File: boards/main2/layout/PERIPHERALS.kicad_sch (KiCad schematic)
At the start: 30 parts, among them Q1 AO3400A, SW1 DSHP04TJGER, SW2 GT-TC048B-H025-L1, SW3 GT-TC048B-H025-L1, SW5 GT-TC048B-H025-L1, U2 GT-USB-7010ASV, U6 USBLC6-2SC6

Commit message: 🍱 Regenerate main2's DRIVERS and PERIPHERALS sheets with the widened USBLC6 and the jumper pin labels
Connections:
- net USBD_N: now also U6.4 (I/O2)
- net USBD_P: now also U6.6 (I/O1)
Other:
- note added: "Addressable LEDs: WS2812C-2020 chain"
- note added: "Buttons: user, reset (NRST), boot (BOOT0)"
- note added: "Buzzer: FUET-5030, low-side switch Q1"
- note added: "Sheet ports"
- note added: "Status LEDs"
- note added: "Strategy DIP switch"
- note added: "USB-C receptacle (ESP32 USB), VBUS sense, ESD"
- title: (none) -> User interface and USB-C
- moved on the sheet: BZ1, C18, C19, C20, C21, C60, C79, D1, D2, D3, D4, D5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

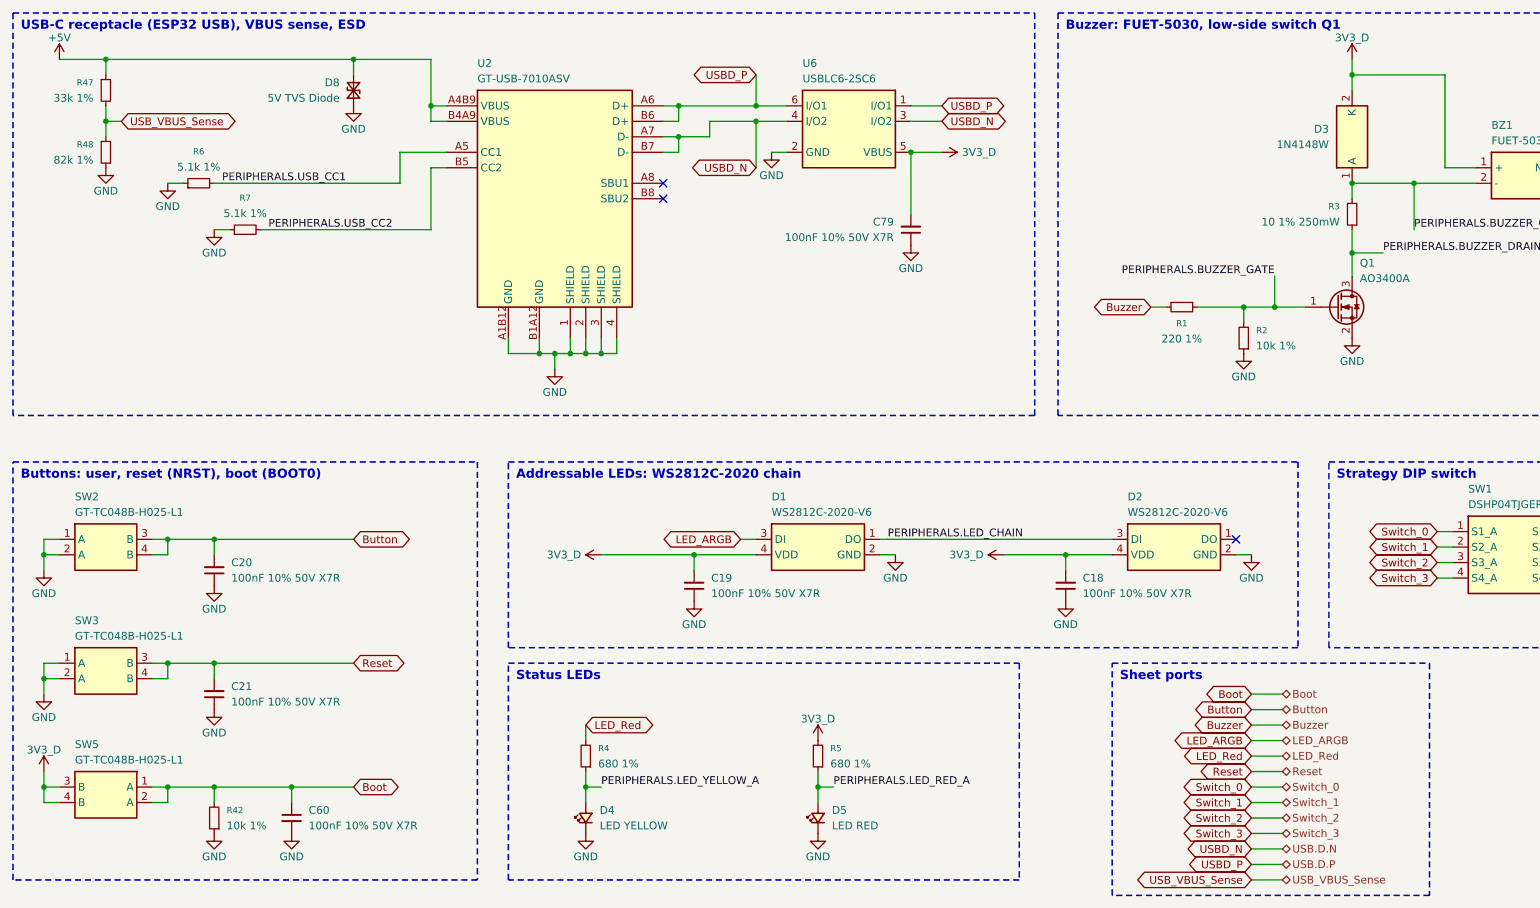
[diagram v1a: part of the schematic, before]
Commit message: ✨ Set main2's emitter current from the DAC and AC-couple its selectors
- The shared sink's set-point comes from PA5 (DAC1_OUT2, buffer off) through
  200k/20k, ratiometric to VDDA and 0 V at reset; 1k/1 nF compensates the loop
  into Q9 and 200k from 3V3_A turns the sink off at a zero set-point.
- Q2-Q5 keep the main board's AC-coupled gates (220 nF, 22k, 1N4148WS clamp):
  a pin held high turns its emitter off within 11 ms.
- Battery_Voltage moves to PC5, Switch_0 to PH0; the H7's VBUS divider goes,
  the ESP32 reports USB power over UART4.
- A test bench checks the selector coupling and the DAC set-point; the
  research model is calculations/emitter/emitter_sink.py.
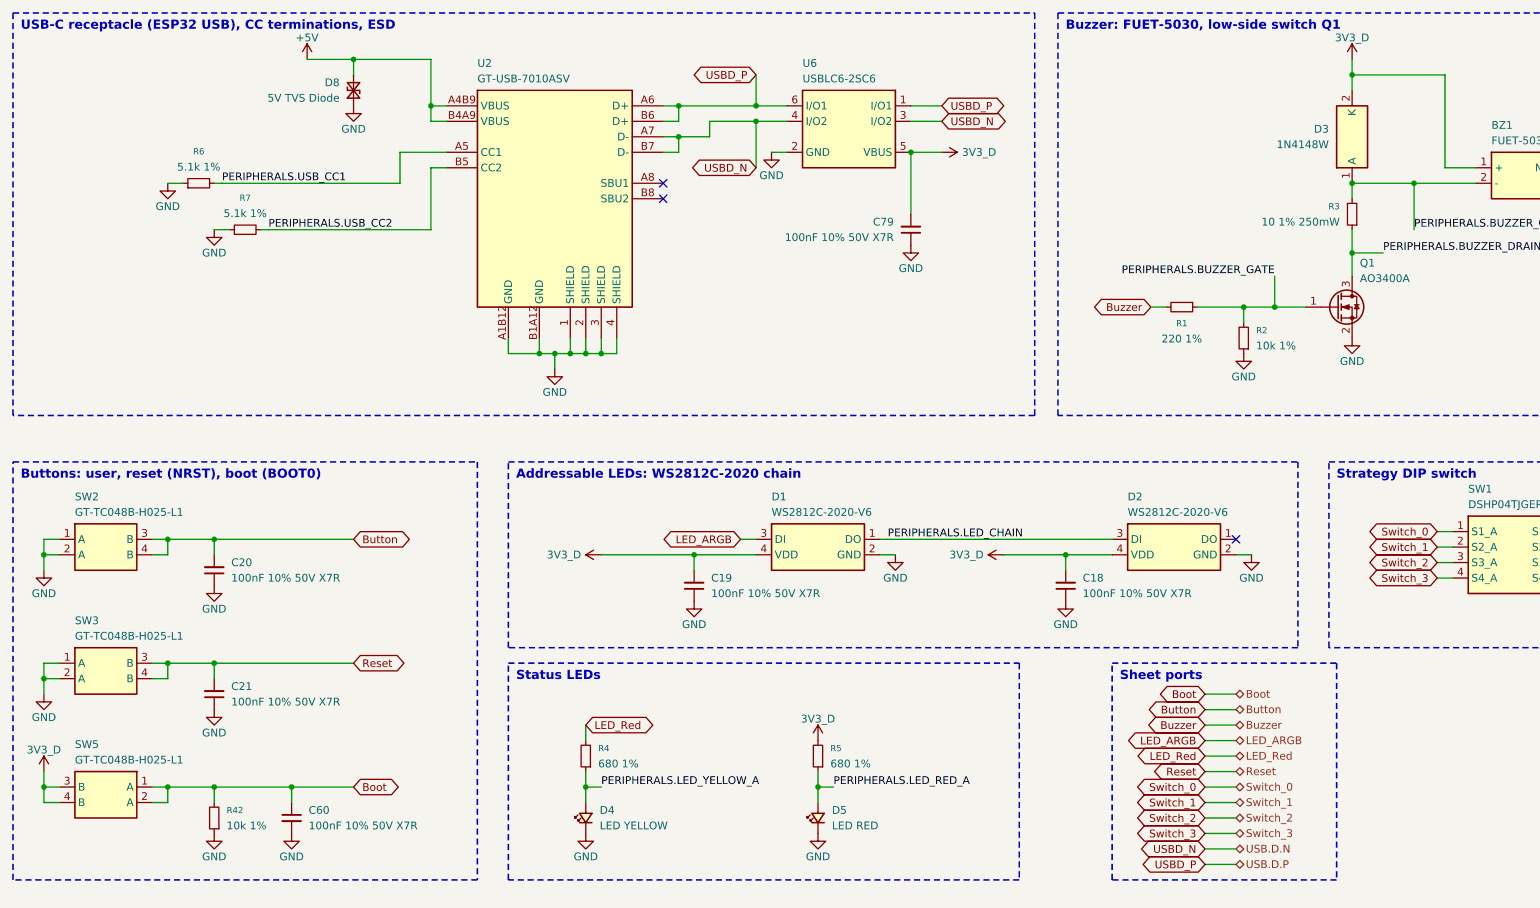
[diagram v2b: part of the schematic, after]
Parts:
- removed R47: 33k 1%, stdlib_kicad-footprints_Resistor_SMD:R_0402_1005Metric, symbol R_Small
- removed R48: 82k 1%, stdlib_kicad-footprints_Resistor_SMD:R_0402_1005Metric, symbol R_Small
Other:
- note added: "USB-C receptacle (ESP32 USB), CC terminations, ESD"
- note removed: "USB-C receptacle (ESP32 USB), VBUS sense, ESD"

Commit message: 🚧 Place and route main2 but for 12 connections
place.py places every part and route.py pours the planes and routes the board, with hand-routed
fixes on top. 12 connections are still open (boards/main2/layout/README.md, Layout), so DRC and
the layout check fail on them; every other gate passes.
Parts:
- removed SW5: GT-TC048B-H025-L1, Team-Micras_MicrasPCB_components_g-switch_GT-TC048B-H025-L1:SW-SMD-4P_L4.2-W3.2_GT-TC048, symbol GT-TC048B-H025-L1
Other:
- note added: "Buttons: user, reset (NRST); BOOT0 pull-down"
- note removed: "Buttons: user, reset (NRST), boot (BOOT0)"

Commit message: 🐛 Fix main2's review findings and settle its open doubts
Schematic and parts:
- Battery input: F1 is a 12 A Littelfuse 501 (0501012.WR1). C58 now sits
  gate-source with C114 gate-drain, so Q6 stays off at plug-in. D16 clamps
  Q8's VGS. R44/R45 are 10k/2k, so VBAT can't float up on USB alone.
- Capacitors: VBAT and VSYS use 1210/0805 50 V parts, sized with Samsung's
  DC-bias curves. C109 is fitted.
- Drivers: R66/R76 are removed (the chokes are needed). ITRIP and the fan
  limit are retuned. The INA241 R_iso is 150 Ohm.
- Rails are declared as ranges, and the abs-max checks run under the TVS
  clamp.
- STM32 pin swaps for routing: the wall selectors move to TIM3,
  Motor_Left_EN to TIM8_CH2 and LED_ARGB to TIM17. CubeMX 6.18.1 confirms
  the map.
- firmware_changes.toml registers the matching firmware changes: the ADC
  0.7 us sampling time, the TIM4-triggered DAC, the fan's 50 kHz start, a
  wheel-sign self-check, VDDA tracking, contest mode, the debug halt and
  others.

Layout:
- USB D+/D- are routed as a coupled pair. The track floor is 0.12 mm.
- Stubs and detours are trimmed. The In2 VCORE/3V3_D islands are shrunk.
- The board is notched under the ESP32 antenna.
- Ground stitching, thermal reliefs, open thermal vias with split paste,
  DRV8874 heat islands and teardrops are added.
- 11 joins remain for hand-routing (layout README, Open items).

Doubts are closed by datasheets, vendor SPICE models and new research
calculations instead of bench TODOs. Tests cover each review item.
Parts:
- D3: value 1N4148W -> 1N4148WS; footprint Team-Micras_MicrasPCB_components_hongjiacheng_1N4148W:SOD-123_L2.7-W1.6-LS3.7-FD -> Team-Micras_MicrasPCB_components_cj_1N4148WS:D_SOD-323; symbol 1N4148W -> 1N4148WS
- D8: value 5V TVS Diode -> 6V TVS Diode
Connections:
- net 3V3_D: now also D3.1 (K); no longer D3.2 (K)
- net PERIPHERALS.BUZZER_COIL: now also D3.2 (A); no longer D3.1 (A)
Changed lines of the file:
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@@
 	)
 	(symbol
-		(lib_id "1N4148W")
+		(lib_id "1N4148WS")
 		(at 229.87 33.02 90)
 		(unit 1)
@@
 			)
 		)
-		(property "Value" "1N4148W"
+		(property "Value" "1N4148WS"
 			(at 226.06 34.29 90)
 			(show_name no)
@@
 			)
 		)
-		(property "Footprint" "Team-Micras_MicrasPCB_components_hongjiacheng_1N4148W:SOD-123_L2.7-W1.6-LS3.7-FD"
+		(property "Footprint" "Team-Micras_MicrasPCB_components_cj_1N4148WS:D_SOD-323"
 			(at 229.87 33.02 90)
 			(hide yes)
@@
 			)
 		)
-		(property "Datasheet" "https://www.lcsc.com/product-detail/C7420318.html"
+		(property "Datasheet" "https://www.lcsc.com/datasheet/lcsc_datasheet_1810101110_Jiangsu-Changjing-Electronics-Technology-Co---Ltd--1N4148WS_C2128.pdf"
 			(at 229.87 33.02 90)
 			(hide yes)
@@
 			)
 		)
-		(property "Description" "Fast switching diode, 100 V, 150 mA, trr 4 ns, SOD-123 (pad 1 anode, pad 2 cathode)"
+		(property "Description" "Fast switching diode, 100 V, 150 mA, trr 4 ns, SOD-323 (pad 1 cathode, pad 2 anode)"
 			(at 229.87 33.02 90)
 			(hide yes)
@@
 			)
 		)
-		(property "Value" "5V TVS Diode"
+		(property "Value" "6V TVS Diode"
 			(at 63.754 26.67 90)
 			(show_name no)
@@
 			)
 		)
-		(property "Description" "5V TVS Diode"
+		(property "Description" "6V TVS Diode"
 			(at 66.04 25.4 90)
 			(hide yes)

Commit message: 🎨 Draw the diodes and buzzer as symbols, and make D4 blue
- 1N4148WS, B5819W and FUET-5030: replace the box bodies with diode,
  Schottky and buzzer symbols (same pins). Nudge D3 and BZ1 on both boards'
  PERIPHERALS sheets.
- D4: KENTO KT-0603B blue (C2288, VF 2.6-3.1 V at 5 mA) instead of the
  yellow NCD0603Y2. R4 goes from 680 Ohm to 100 Ohm: 1.2 mA at the worst
  bin and rail, 7.5 mA at most. LED_YELLOW_A is renamed LED_BLUE_A.
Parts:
- D4: value LED YELLOW -> LED BLUE; symbol LED_Small_Filled_Yellow -> LED_Small_Filled_Blue
- R4: value 680 1% -> 100 1%
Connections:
- net PERIPHERALS.LED_YELLOW_A renamed PERIPHERALS.LED_BLUE_A
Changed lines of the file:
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@@
 	(symbol
 		(lib_id "FUET-5030")
-		(at 257.81 40.64 0)
+		(at 257.81 38.1 0)
 		(unit 1)
 		(body_style 1)
@@
 		(dnp no)
 		(property "Reference" "BZ1"
-			(at 252.73 31.115 0)
+			(at 256.159 30.48 0)
 			(show_name no)
 			(do_not_autoplace no)
@@
 		)
 		(property "Value" "FUET-5030"
-			(at 252.73 33.655 0)
+			(at 256.159 33.02 0)
 			(show_name no)
 			(do_not_autoplace no)
@@
 		)
 		(property "Footprint" "Team-Micras_MicrasPCB_components_fuet_FUET-5030:BUZ-SMD_FST-5030"
-			(at 257.81 40.64 0)
+			(at 257.81 38.1 0)
 			(hide yes)
 			(show_name no)
@@
 		)
 		(property "Datasheet" "https://www.lcsc.com/product-detail/C391031.html"
-			(at 257.81 40.64 0)
+			(at 257.81 38.1 0)
 			(hide yes)
 			(show_name no)
@@
 		)
 		(property "Description" "4 kHz passive electromagnetic buzzer, 3 Vo-p rated, 12 ohm coil, 5 x 5 x 3 mm SMD (pad 3 mechanical, no electrical function stated)"
-			(at 257.81 40.64 0)
+			(at 257.81 38.1 0)
 			(hide yes)
 			(show_name no)
@@
 		)
 		(property "Path" "PERIPHERALS.BZ1.BUZZER"
-			(at 257.81 40.64 0)
+			(at 257.81 38.1 0)
 			(hide yes)
 			(show_name no)
@@
 	)
 	(symbol
-		(lib_id "LED_Small_Filled_Yellow")
+		(lib_id "LED_Small_Filled_Blue")
 		(at 104.14 144.78 90)
 		(unit 1)
@@
 			)
 		)
-		(property "Value" "LED YELLOW"
+		(property "Value" "LED BLUE"
 			(at 106.426 146.05 90)
 			(show_name no)
@@
 			)
 		)
-		(property "Description" "LED YELLOW"
+		(property "Description" "LED BLUE"
 			(at 104.14 144.78 90)
 			(hide yes)
@@
 			)
 		)
-		(property "Value" "680 1%"
+		(property "Value" "100 1%"
 			(at 106.172 135.89 0)
 			(show_name no)
@@
 			)
 		)
-		(property "Description" "680 1%"
+		(property "Description" "100 1%"
 			(at 104.14 134.62 0)
 			(hide yes)
@@
 	(symbol
 		(lib_id "1N4148WS")
-		(at 229.87 33.02 90)
+		(at 229.87 36.83 90)
 		(unit 1)
 		(body_style 1)
@@
 		(dnp no)
 		(property "Reference" "D3"
-			(at 226.06 31.75 90)
+			(at 227.33 35.56 90)
 			(show_name no)
 			(do_not_autoplace no)
@@
 		)
 		(property "Value" "1N4148WS"
-			(at 226.06 34.29 90)
+			(at 227.33 38.1 90)
 			(show_name no)
 			(do_not_autoplace no)
@@
 		)
 		(property "Footprint" "Team-Micras_MicrasPCB_components_cj_1N4148WS:D_SOD-323"
-			(at 229.87 33.02 90)
+			(at 229.87 36.83 90)
 			(hide yes)
 			(show_name no)
@@
 		)
 		(property "Datasheet" "https://www.lcsc.com/datasheet/lcsc_datasheet_1810101110_Jiangsu-Changjing-Electronics-Technology-Co---Ltd--1N4148WS_C2128.pdf"
-			(at 229.87 33.02 90)
+			(at 229.87 36.83 90)
 			(hide yes)
 			(show_name no)
@@
 		)
 		(property "Description" "Fast switching diode, 100 V, 150 mA, trr 4 ns, SOD-323 (pad 1 cathode, pad 2 anode)"
-			(at 229.87 33.02 90)
+			(at 229.87 36.83 90)
 			(hide yes)
 			(show_name no)
@@
 		)
 		(property "Path" "PERIPHERALS.D3.D"
-			(at 229.87 33.02 90)
+			(at 229.87 36.83 90)
 			(hide yes)
 			(show_name no)
@@
 	)
 	(no_connect
-		(at 265.43 38.1)
+		(at 262.89 38.1)
 	)
 	(no_connect
@@
 	(wire
 		(pts
-			(xy 229.87 25.4) (xy 229.87 22.86)
+			(xy 229.87 33.02) (xy 229.87 22.86)
 		)
 		(stroke
@@
 	(wire
 		(pts
-			(xy 250.19 38.1) (xy 245.11 38.1)
+			(xy 255.27 35.56) (xy 245.11 35.56)
 		)
 		(stroke
@@
 	(wire
 		(pts
-			(xy 245.11 38.1) (xy 245.11 22.86)
+			(xy 245.11 35.56) (xy 245.11 22.86)
 		)
 		(stroke
@@
 	(wire
 		(pts
-			(xy 250.19 40.64) (xy 240.03 40.64)
+			(xy 255.27 40.64) (xy 240.03 40.64)
 		)
 		(stroke
@@
 		)
 	)
-	(label "PERIPHERALS.LED_YELLOW_A"
+	(label "PERIPHERALS.LED_BLUE_A"
 		(at 106.68 139.7 0)
 		(effects

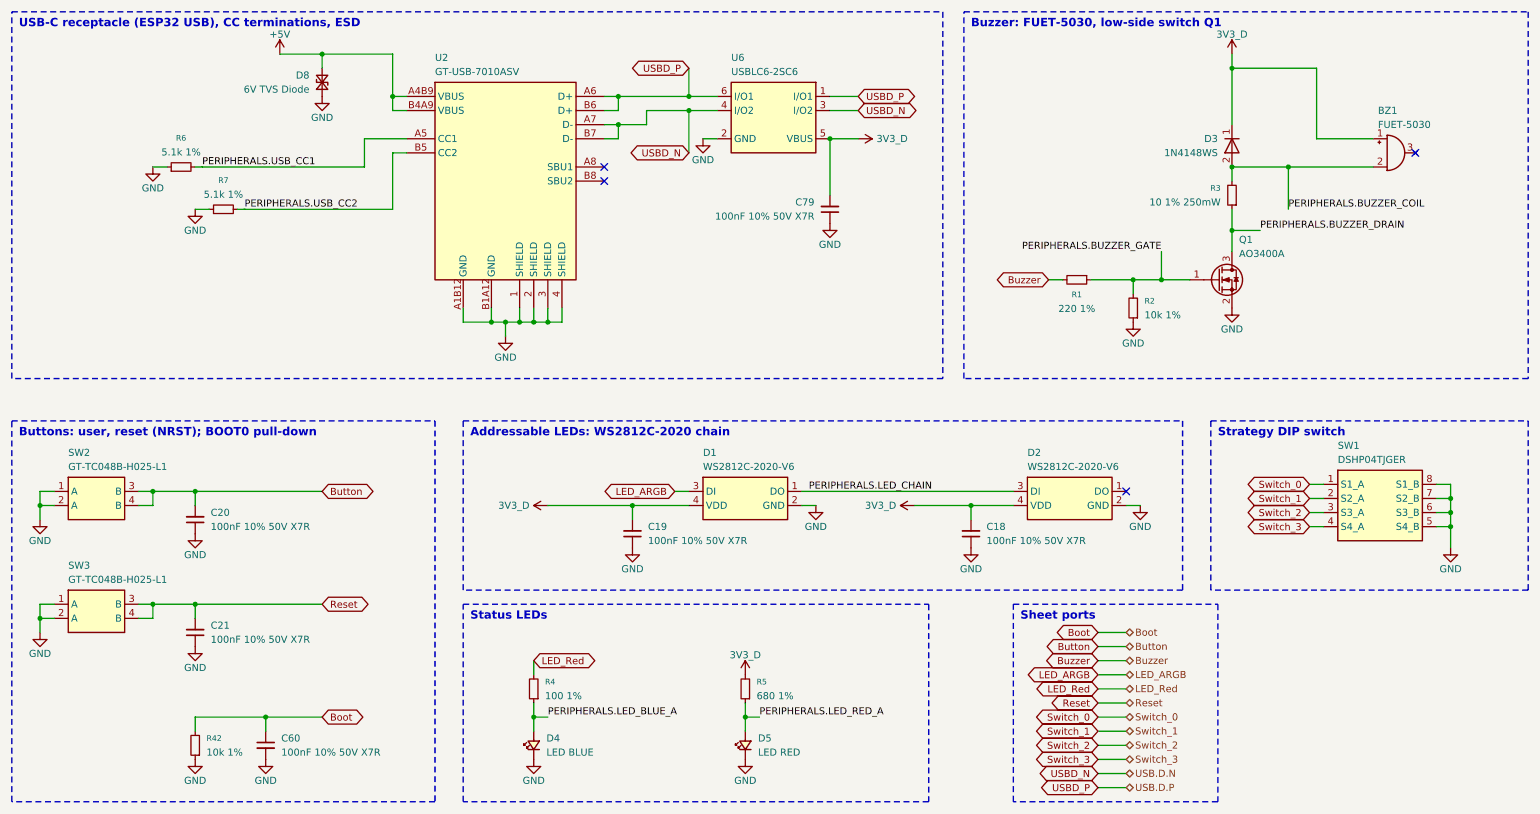
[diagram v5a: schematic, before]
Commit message: 🚧 Swap main2's USB and ESP32-S3 for an ESP32-C5 and programming headers
Schematic and component checkpoint; the layout follows in its own commit.

- Remove USB-C, its ESD, power path and VBUS sense; both MCUs flash over
  the air.
- U13 ESP32-C5-MINI-1-N4 (dual-band, 5 GHz channels 36-48) in the
  rear-right corner, with its antenna notch on the right edge. SW4 and its
  notch move to the rear-left.
- H7-C5 link: SPI2 half-duplex 3-wire (PA12 SCK, PA11 CSn, PB14 DATA with
  IOSWP), PA9 flow control, UART4 fallback on the same pins. Fan_Enable
  moves to PB10, IMU INT1 to PB6, INT2 is left open.
- J2: 2x3 1.27 mm header in the ESP-Prog layout. SWD1: 1x4 1.27 mm in
  clone ST-Link order (SWDIO, GND, SWCLK, 5V). 5V_IN feeds VSYS through
  D17 (B5819W) to flash without the battery.
- R44/R45 to 20k/2k keeps PC5 below its absolute maximum at the clamp.
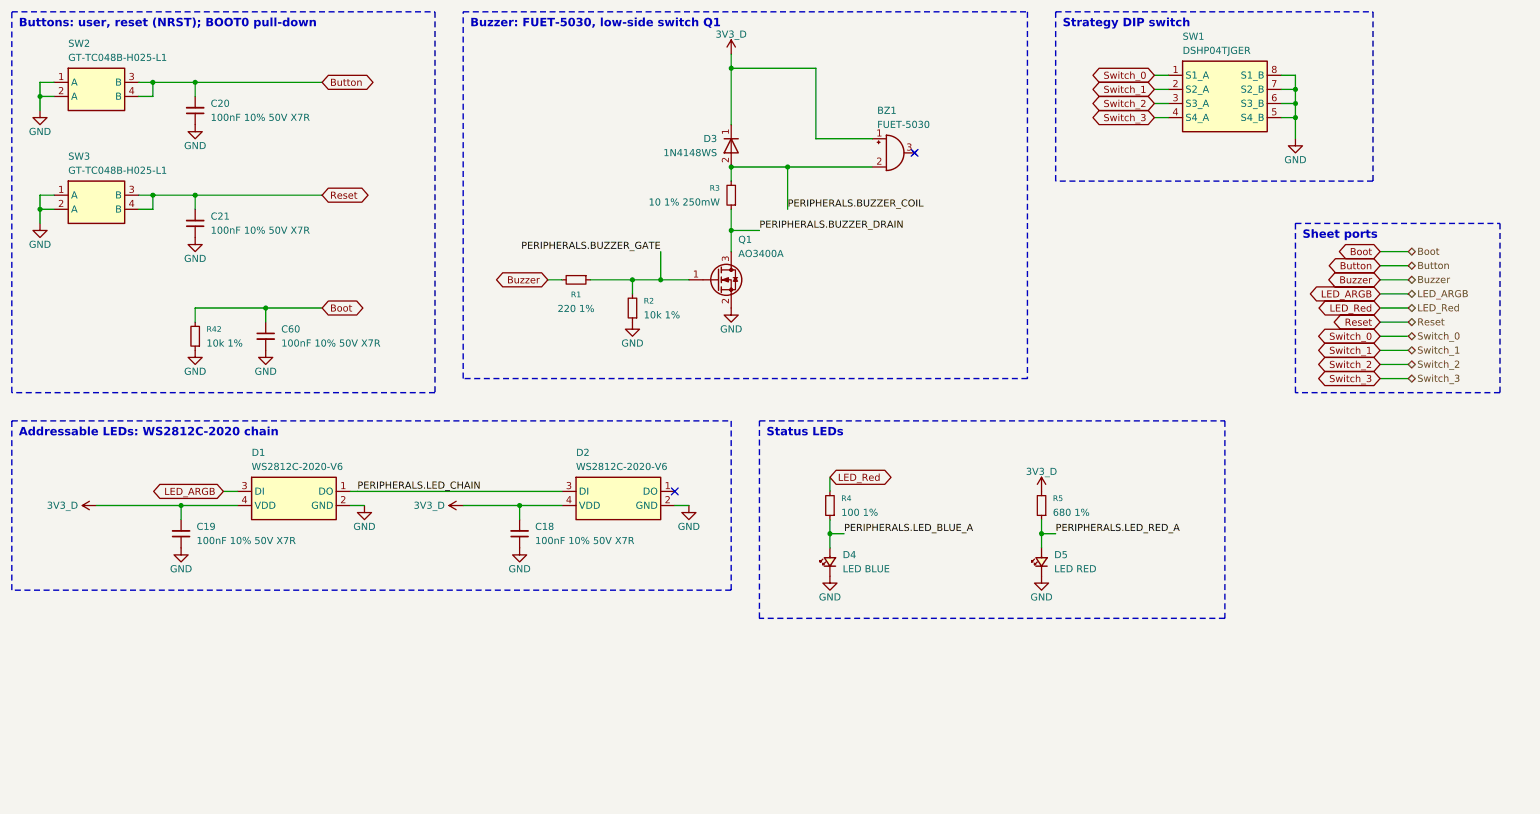
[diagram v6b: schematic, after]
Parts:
- removed C79: 100nF 10% 50V X7R, stdlib_kicad-footprints_Capacitor_SMD:C_0402_1005Metric, symbol C_Small
- removed D8: 6V TVS Diode, stdlib_kicad-footprints_Diode_SMD:D_SOD-882, symbol D_TVS_Small
- removed R6, R7: 5.1k 1%, stdlib_kicad-footprints_Resistor_SMD:R_0402_1005Metric, symbol R_Small
- removed U2: GT-USB-7010ASV, Team-Micras_MicrasPCB_components_g-switch_GT-USB-7010ASV:USB-C_G-Switch_GT-USB-7010ASV, symbol GT-USB-7010ASV
- removed U6: USBLC6-2SC6, Team-Micras_MicrasPCB_components_st_USBLC6-2SC6:SOT-23-6_ST_USBLC6-2SC6, symbol USBLC6-2SC6
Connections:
- no-connect marks 4 -> 2
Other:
- note removed: "USB-C receptacle (ESP32 USB), CC terminations, ESD"
- title: User interface and USB-C -> User interface
- moved on the sheet: BZ1, C18, C19, C20, C21, C60, D1, D2, D3, D4, D5, Q1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
